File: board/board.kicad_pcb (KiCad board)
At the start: 2 copper layers, 60 x 30 mm, 73 parts, among them IC1 NC7SZ11P6X, IC2 FM25L16B-DG, IC3 NCP189CMTW330TAG, J1 USB, J2 Conn_01x12, J3 Conn_01x03, J4 MEM2085-00-115-00-A, SW1 SW_Push, SW2 SW_Push, U1 MT9M001C12STM, U2 APS6404L-3SQR-ZR, U3 RP2350_60QFN, Y1 ABM8-272-T3

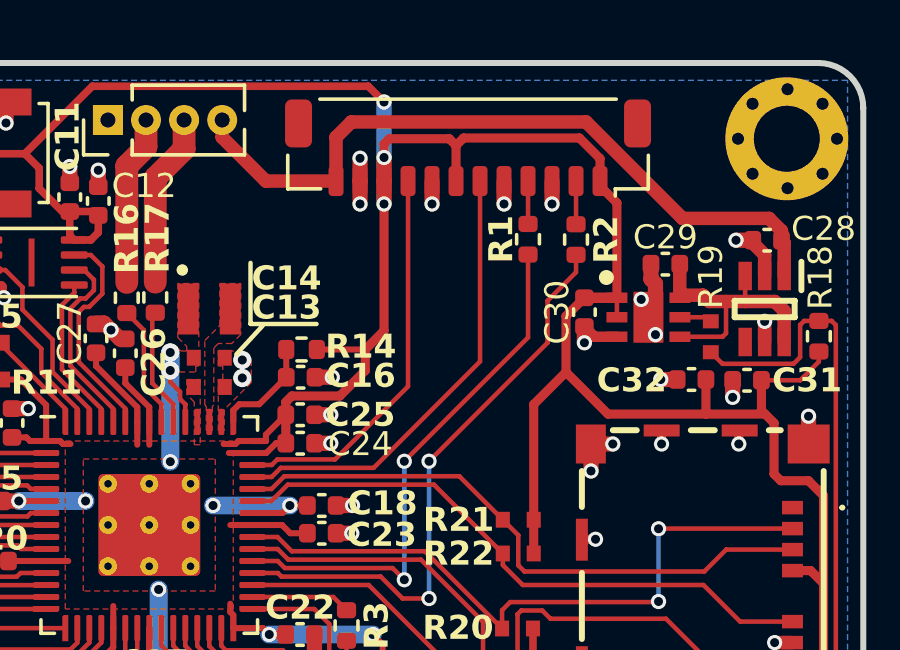
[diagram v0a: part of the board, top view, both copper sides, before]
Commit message: use embassy, implement minor script improvements, and make minor pcb improvements
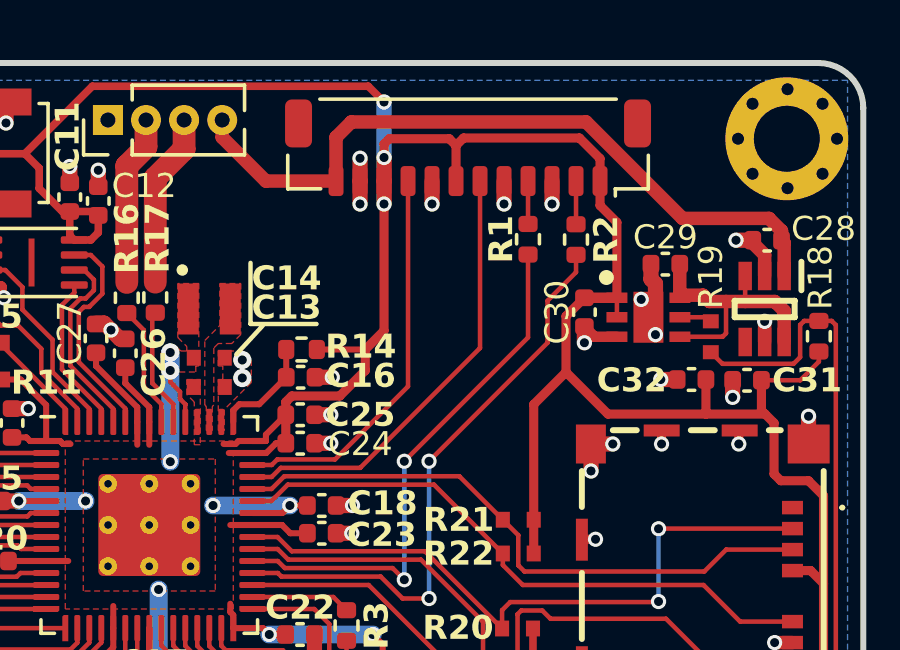
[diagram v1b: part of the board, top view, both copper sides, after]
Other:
- board text added: "2025/12"
- board text removed: "2025/10"
